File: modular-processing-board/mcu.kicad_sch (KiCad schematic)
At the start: 47 parts, among them J202 Conn_02x06_Odd_Even, SW201 SW_Push, SW602 SW_Push, U201 STM32H723ZGTx, Y1201 25MHz

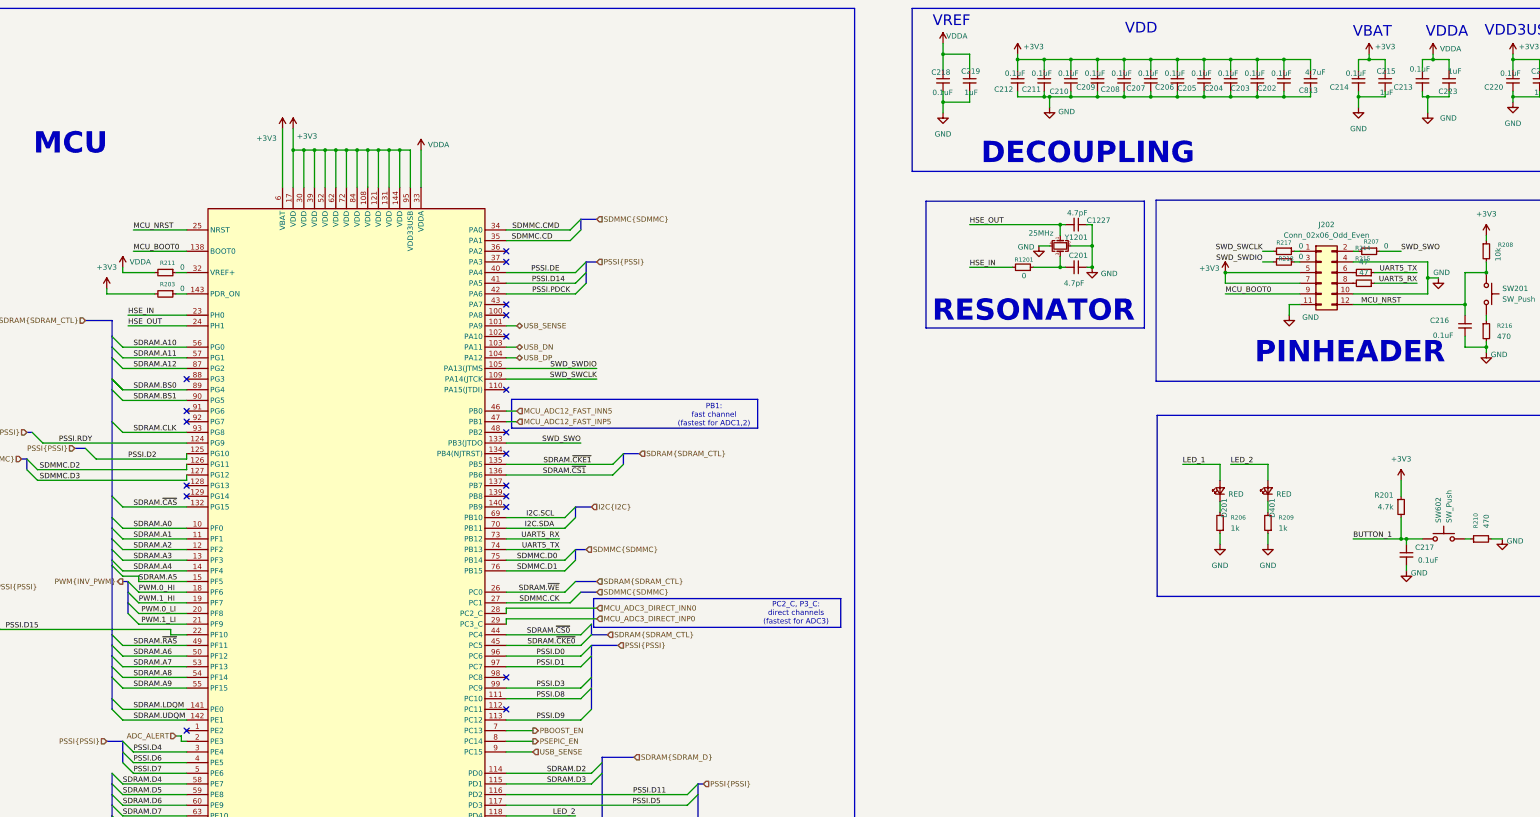
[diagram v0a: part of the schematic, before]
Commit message: reconnected vref
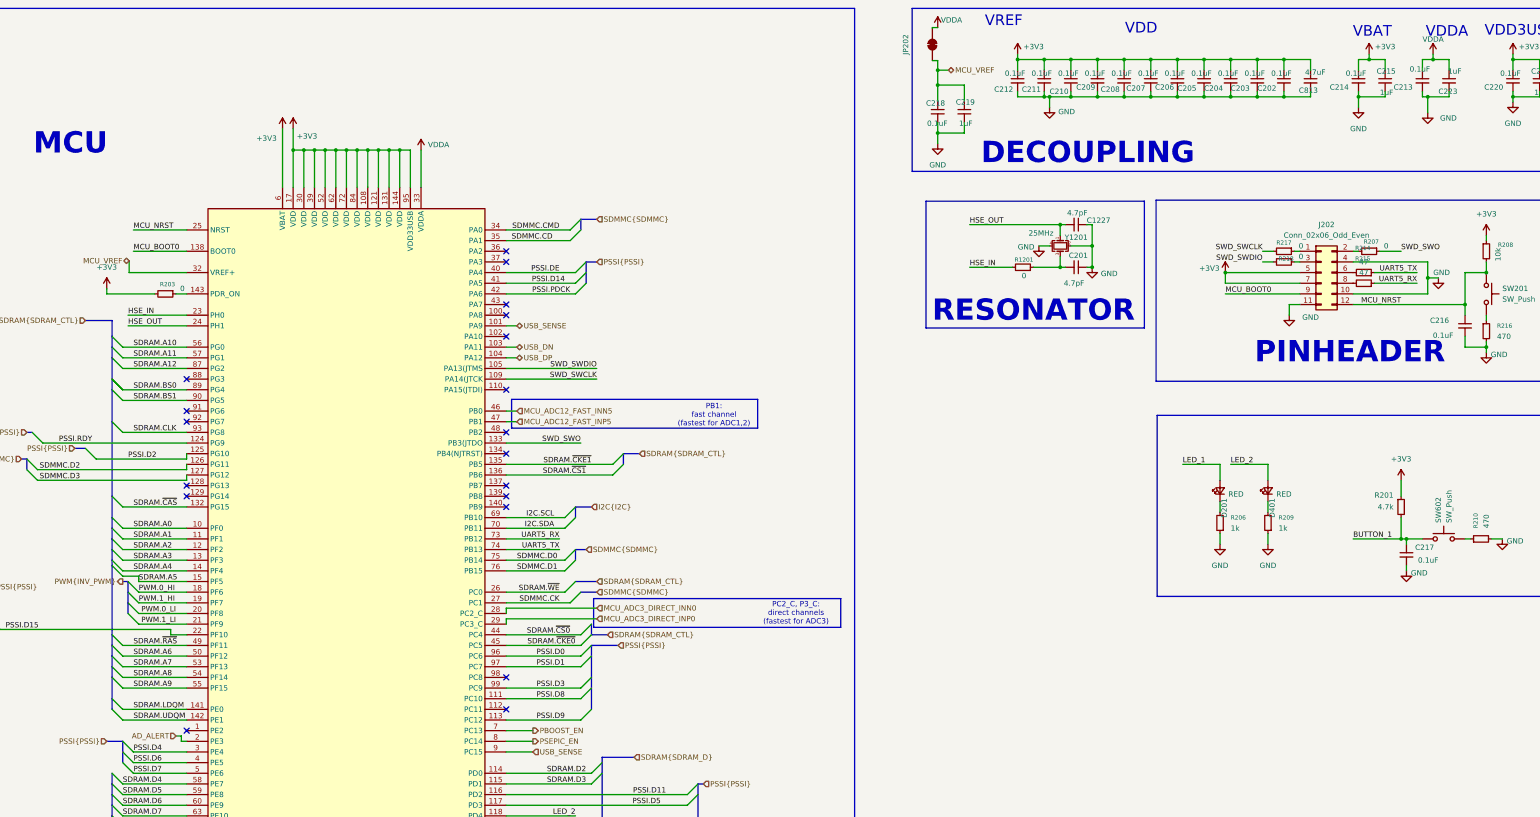
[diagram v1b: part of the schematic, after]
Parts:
- removed R211: 0, Resistor_SMD:R_0805_2012Metric_Pad1.20x1.40mm_HandSolder, symbol Device:R_Small
- added JP202: SolderJumper_2_Bridged, Jumper:SolderJumper-2_P1.3mm_Bridged2Bar_Pad1.0x1.5mm, symbol Jumper:SolderJumper_2_Bridged
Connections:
- net VDDA: now also JP202.2 (B); no longer C218.1, C219.1
- net MCU_VREF: now reaches U201.32 (VREF+)
- net MCU_VREF: now also C218.1, C219.1, JP202.1 (A)
- net ADC_ALERT renamed AD_ALERT
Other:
- moved on the sheet: C218, C219

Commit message: layed out most components (next) cadd vias for impedance reduction for high-speed signals, check impedance of signals
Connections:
- net USB_SENSE: no longer U201.9 (PC15)
- no-connect marks 20 -> 21

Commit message: completed schematic + layout (next) do footprint checks etc.
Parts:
- added TP201, TP202: TestPoint, iw-misc:TestPoint_Pad_D0.5mm, symbol Connector:TestPoint
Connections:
- net +3V3: now also TP201.1
- net VDDA: now also TP202.1

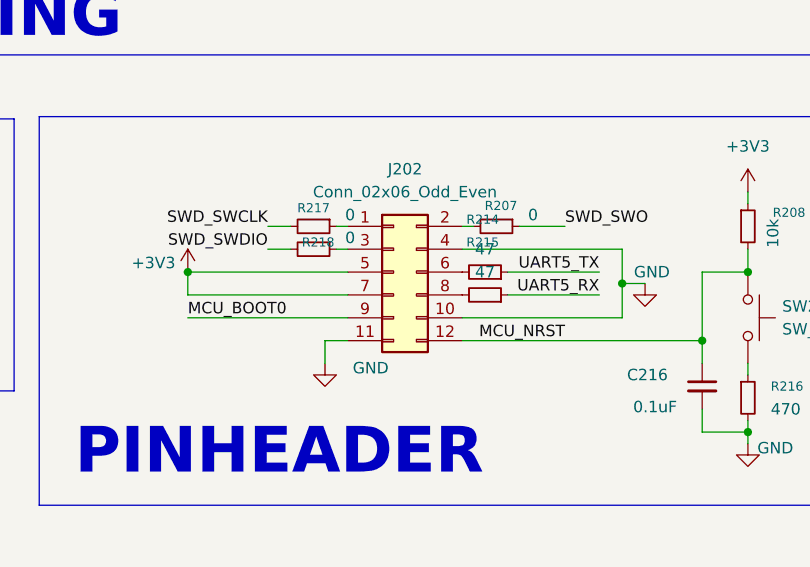
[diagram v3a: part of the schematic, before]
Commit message: checking SDMMC SD-card interface (next) finish checking sd-card holder, check connectors, frontend and power
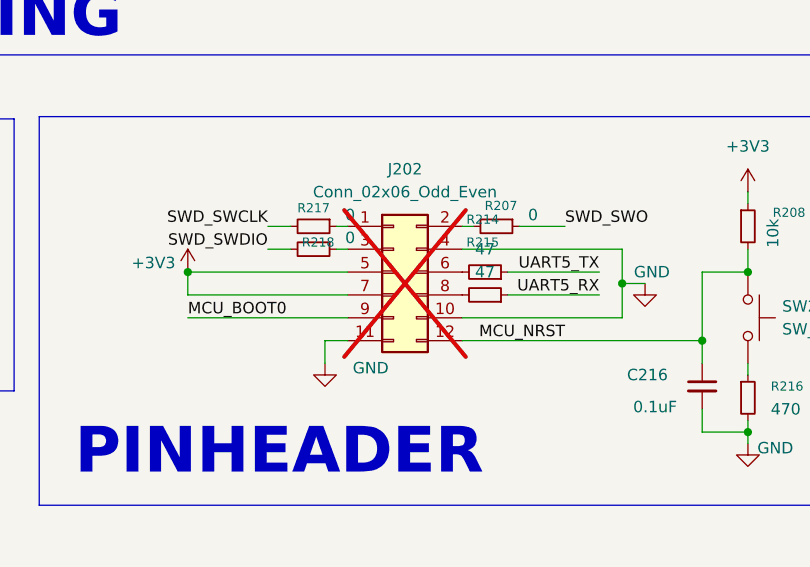
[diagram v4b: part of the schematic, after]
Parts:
- C222, C224: LCSC Part Number C22435929 -> (none); Manufacturing Part Number CGA0201X7R104K160ET -> (none)
- J202: now not fitted; now left out of the parts list

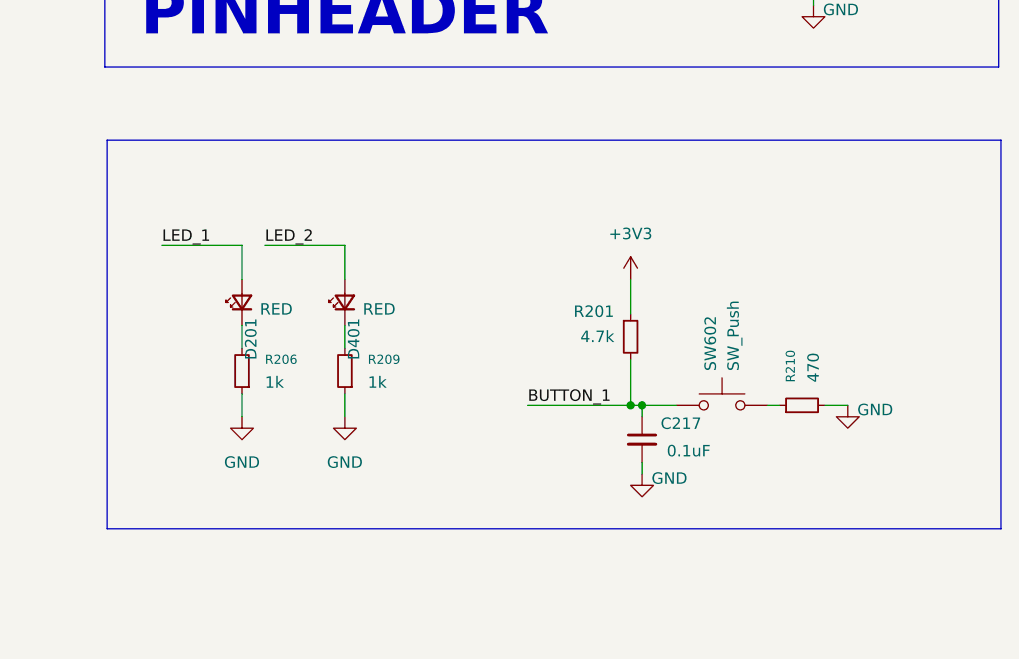
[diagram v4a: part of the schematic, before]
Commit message: checked components part numbers (next) board checks
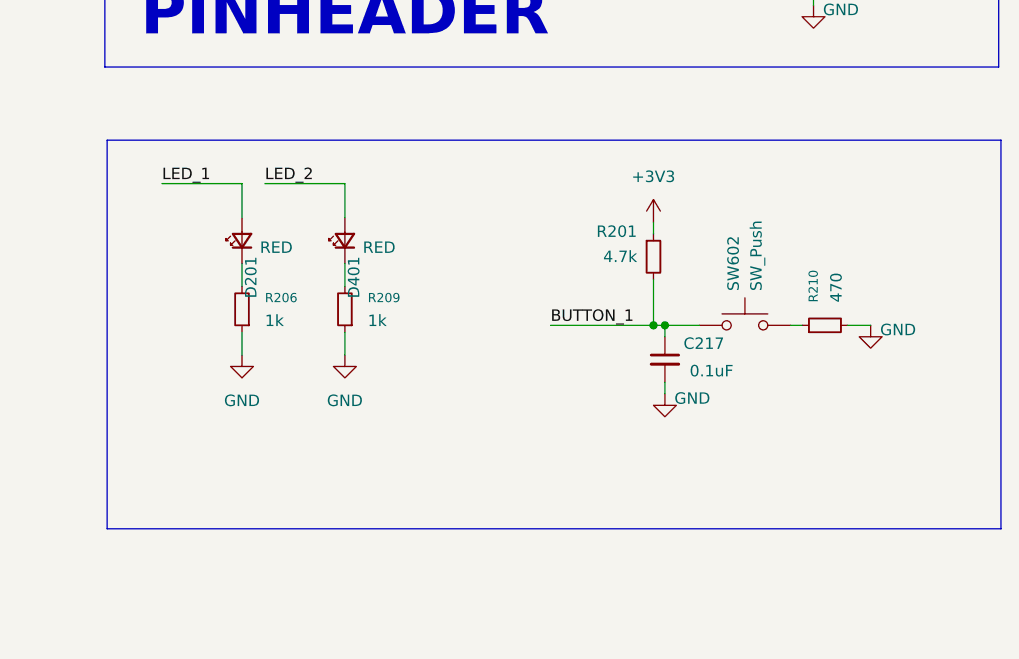
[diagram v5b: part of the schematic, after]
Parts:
- C215, C219, C221, C223: LPN (none) -> C28323; MPN (none) -> CL21B105KBFNNNE
- C813: LPN (none) -> C23733; MPN (none) -> CL05A475MP5NRNC
- D201, D401: LPN (none) -> C2286; MPN (none) -> KT-0603R
- R1201: LPN (none) -> C17168; MPN (none) -> 0402WGF0000TCE
- R201: LPN (none) -> C25900; MPN (none) -> 0402WGF4701TCE
- R203, R207, R217, R218: LPN (none) -> C17477; MPN (none) -> 0805W8F0000T5E
- R206, R209: LPN (none) -> C11702; MPN (none) -> 0402WGF1001TCE
- R208: LPN (none) -> C25804; MPN (none) -> 0603WAF1002T5E
- R210, R216: LPN (none) -> C25117; MPN (none) -> 0402WGF4700TCE
- R214, R215: LPN (none) -> C23182; MPN (none) -> 0603WAF470JT5E
- SW201, SW602: LPN (none) -> C720477; MPN (none) -> TS-1088-AR02016
- Y1201: LPN (none) -> C9006; MPN (none) -> X322525MOB4SI
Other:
- moved on the sheet: C217, D201, D401, R201, R206, R209, R210, SW602

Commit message: matched PSSI bus lenghts
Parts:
- C1227, C201: LCSC Part Number C1569 -> (none); Manufacturing Part Number 0402CG4R7C500NT -> (none)
- C202, C203, C204, C205, C206, C207, C208, C209, C210, C211, C212, C213, C214, C216, C217, C218, C220: LCSC Part Number C22435929 -> (none); Manufacturing Part Number CGA0201X7R104K160ET -> (none)
- C215, C219, C221, C223: LCSC Part Number C28323 -> (none); Manufacturing Part Number CL21B105KBFNNNE -> (none)
- C813: LCSC Part Number C23733 -> (none); Manufacturing Part Number CL05A475MP5NRNC -> (none)
- D201, D401: LCSC Part Number C2286 -> (none); Manufacturing Part Number KT-0603R -> (none)
- R1201: LCSC Part Number C17168 -> (none); Manufacturing Part Number 0402WGF0000TCE -> (none)
- R201: LCSC Part Number C25900 -> (none); Manufacturing Part Number 0402WGF4701TCE -> (none)
- R203, R207, R217, R218: LCSC Part Number C17477 -> (none); Manufacturing Part Number 0805W8F0000T5E -> (none)
- R206, R209: LCSC Part Number C11702 -> (none); Manufacturing Part Number 0402WGF1001TCE -> (none)
- R208: LCSC Part Number C25804 -> (none); Manufacturing Part Number 0603WAF1002T5E -> (none)
- R210, R216: LCSC Part Number C25117 -> (none); Manufacturing Part Number 0402WGF4700TCE -> (none)
- R214, R215: LCSC Part Number C23182 -> (none); Manufacturing Part Number 0603WAF470JT5E -> (none)
- SW201, SW602: LCSC Part Number C720477 -> (none); Manufacturing Part Number TS-1088-AR02016 -> (none)
- Y1201: LCSC Part Number C9006 -> (none); Manufacturing Part Number X322525MOB4SI -> (none)

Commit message: checked differential impedances + SDMMC lenghts (next) check impedances of SE-signals
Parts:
- C1227, C201: LPN (none) -> C1569; MPN (none) -> 0402CG4R7C500NT

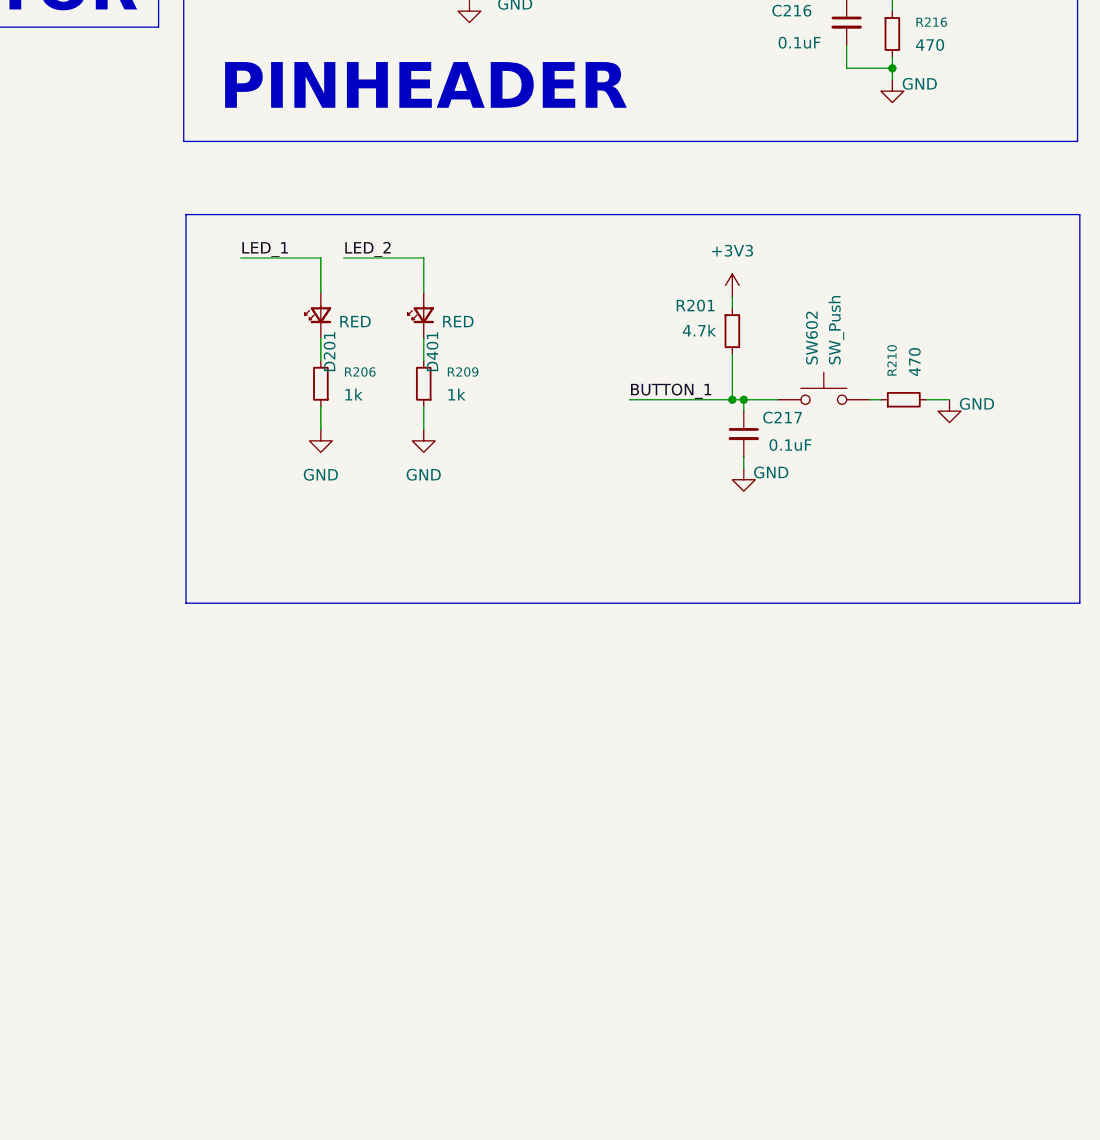
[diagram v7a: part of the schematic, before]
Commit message: finish modular-processing-hw board checks, prepare gerbers for manufacturing and perform checks
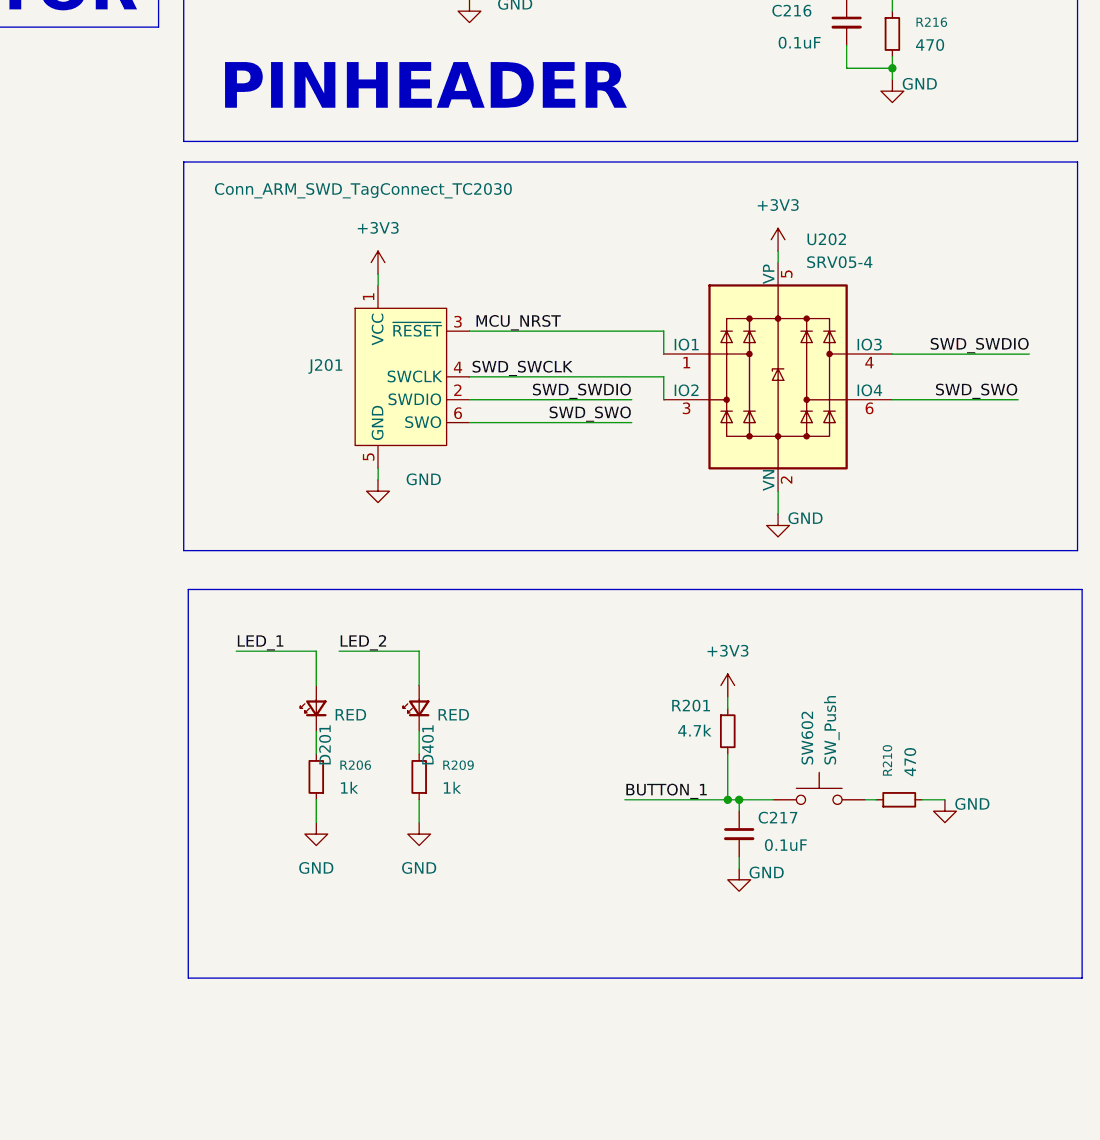
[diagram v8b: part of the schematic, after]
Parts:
- added J201: Conn_ARM_SWD_TagConnect_TC2030, Connector:Tag-Connect_TC2030-IDC-FP_2x03_P1.27mm_Vertical, symbol Connector:Conn_ARM_SWD_TagConnect_TC2030
- added U202: SRV05-4, Package_TO_SOT_SMD:SOT-23-6, symbol Power_Protection:SRV05-4
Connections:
- net +3V3: now also J201.1 (VCC), U202.5 (VP)
- net GND: now also J201.5 (GND), U202.2 (VN)
- net MCU_NRST: now also J201.3 (~{RESET}), U202.1 (IO1)
- net SWD_SWCLK: now also J201.4 (SWCLK), U202.3 (IO2)
- net SWD_SWDIO: now also J201.2 (SWDIO), U202.4 (IO3)
- net SWD_SWO: now also J201.6 (SWO), U202.6 (IO4)
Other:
- moved on the sheet: C217, D201, D401, R201, R206, R209, R210, SW602
